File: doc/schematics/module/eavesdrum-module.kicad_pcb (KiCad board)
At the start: 2 copper layers, 100 x 100 mm, 102 parts, among them J1 DC37_Pins_MountingHoles, J2 Conn_02x25_Odd_Even, J3 Conn_01x03, J4 Conn_01x20_Pin, J5 Conn_01x20_Pin, M4_1 MountingHole_4.3mm_M4, M4_2 MountingHole_4.3mm_M4, M4_3 MountingHole_4.3mm_M4, M4_4 MountingHole_4.3mm_M4, SW1 SW_Push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

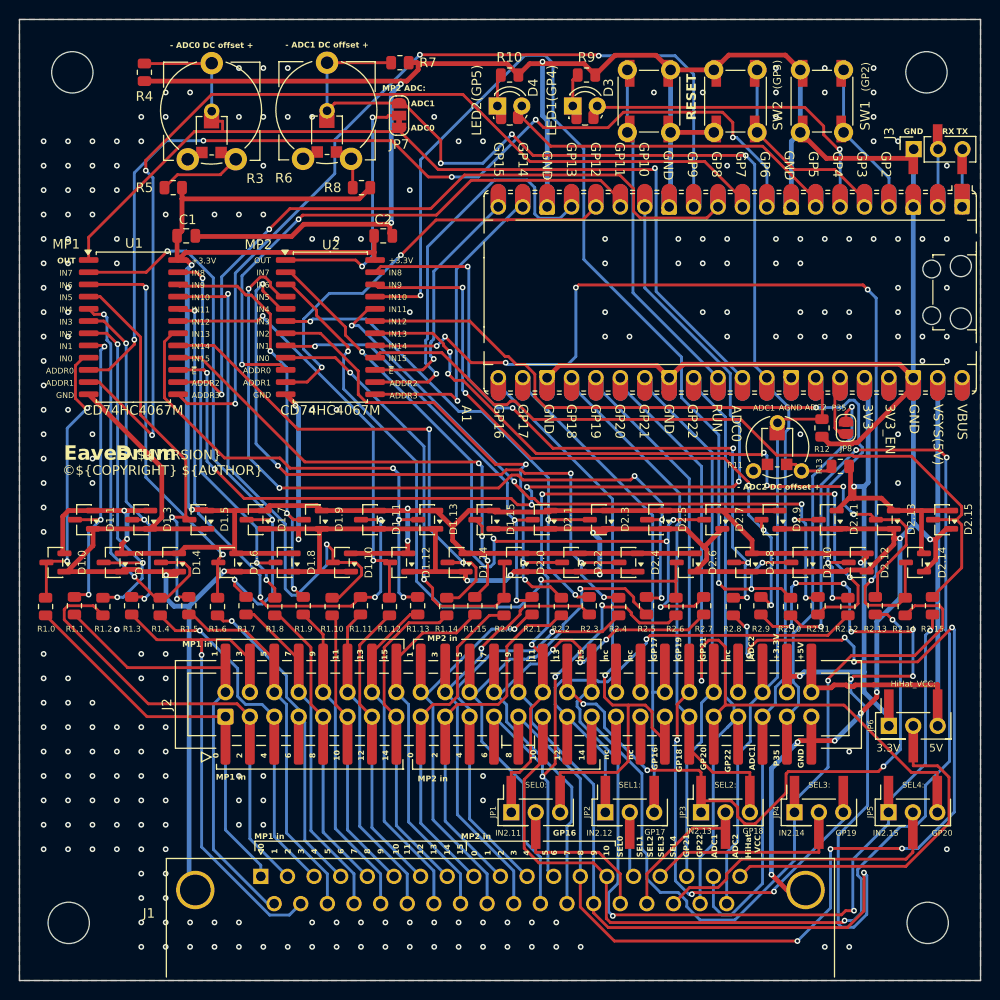
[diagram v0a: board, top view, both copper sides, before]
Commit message: schematics for module 1.2
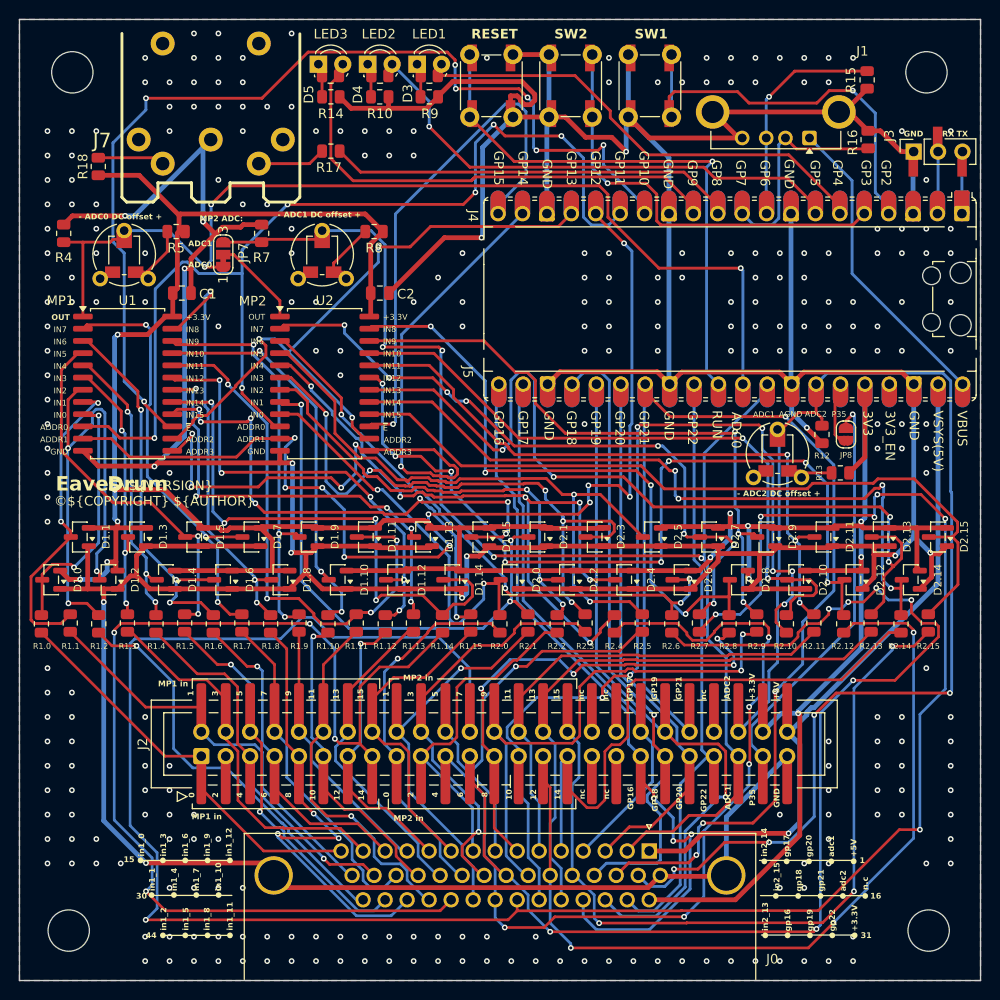
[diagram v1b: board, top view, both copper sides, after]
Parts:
- removed A1: RaspberryPi_Pico, Module:RaspberryPi_Pico_Common_Unspecified
- removed JP1, JP2, JP3, JP4, JP5, JP6: Jumper, Connector_PinHeader_2.54mm:PinHeader_1x03_P2.54mm_Vertical_SMD_Pin1Right
- added D5: LED (yellow), EavesDrum:LED_D3.0mm_SMD_Thru, F.Cu at (97.4, 43.8)
- added J0: SUB-D 44 HD, Connector_Dsub:DSUB-44-HD_Socket_Horizontal_P2.29x2.54mm_EdgePinOffset8.35mm_Housed_MountingHolesOffset10.89mm, F.Cu at (130.5, 124.5)
- added J7: DIN-5_180degree, EavesDrum:MIDI_DIN5, F.Cu at (84.9, 47.5)
- added R14: 4.7k, Resistor_SMD:R_0805_2012Metric, F.Cu at (97.4, 46.1)
- added R15: 15k, Resistor_SMD:R_0805_2012Metric, F.Cu at (153.2, 44.3)
- added R16: 15k, Resistor_SMD:R_0805_2012Metric, F.Cu at (153.3, 50.5)
- added R17: 10, Resistor_SMD:R_0805_2012Metric, F.Cu at (97.4, 51.7)
- added R18: 33, Resistor_SMD:R_0805_2012Metric, F.Cu at (73.2, 53.3)
- D3: footprint LED_THT:LED_D3.0mm -> EavesDrum:LED_D3.0mm_SMD_Thru
- D4: value LED (blue) -> LED (white/blue); footprint LED_THT:LED_D3.0mm -> EavesDrum:LED_D3.0mm_SMD_Thru
- J1: value DC37_Pins_MountingHoles -> USB_A; footprint Connector_Dsub:DSUB-37_Pins_Horizontal_P2.77x2.84mm_EdgePinOffset7.70mm_Housed_MountingHolesOffset9.12mm -> Connector_USB:USB_A_Connfly_DS1095
- J2: footprint Connector_IDC:IDC-Header_2x25_P2.54mm_Vertical -> EavesDrum:IDC-Header_2x25_P2.54mm_Vertical_SMD_Thru
- J3: footprint Connector_PinSocket_2.54mm:PinSocket_1x03_P2.54mm_Vertical_SMD_Pin1Left -> EavesDrum:PinSocket_1x03_P2.54mm_Vertical_SMD_Thru_Pin1Left
- J4: value Conn_01x20_Pin -> Conn_01x20_Socket; footprint Connector_PinSocket_2.54mm:PinSocket_1x20_P2.54mm_Vertical -> EavesDrum:RaspberryPi_Pico_wo_2nd_pin_row
- J5: value Conn_01x20_Pin -> Conn_01x20_Socket; footprint Connector_PinSocket_2.54mm:PinSocket_1x20_P2.54mm_Vertical -> EavesDrum:RaspberryPi_Pico_Common_2nd_pin_row
- R10: value 4.7k -> 10k
- R11, R3, R6: footprint Potentiometer_SMD:Potentiometer_ACP_CA9-VSMD_Vertical -> EavesDrum:Potentiometer_SMD_Thru_Vertical
- SW1, SW2, SW3: footprint Button_Switch_SMD:SW_Push_1P1T_NO_CK_KSC6xxJ -> EavesDrum:SW_Push_SMD_Thru
- moved J1 95.7 mm to (147.2, 50.3), turned to 180 degrees
- moved J5 25.6 mm to (139.0, 67.1), turned to -90 degrees
- moved J4 24.2 mm to (138.9, 58.2)
- moved JP7 23.3 mm to (86.2, 62.5)
- moved R7 22.9 mm to (90.2, 60.3), turned to -90 degrees
- moved R4 18.7 mm to (69.6, 60.3), turned to -90 degrees
- moved SW1 18.0 mm to (130.6, 44.9)
- moved SW2 17.2 mm to (122.3, 44.9)
- moved D3 16.8 mm to (107.6, 43.8)
- moved R9 16.5 mm to (107.6, 46.1)
- moved SW3 16.5 mm to (114.1, 44.9)
- moved D4 14.2 mm to (102.5, 43.8)
- moved R10 13.7 mm to (102.5, 46.1)
- moved R3 13.5 mm to (75.9, 60.0)
- moved R6 10.1 mm to (96.5, 60.0)
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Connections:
- J1 pad 1: /in1_0 -> Vbus
- J1 pad 2: /in1_2 -> gpio7
- J1 pad 3: /in1_4 -> gpio6
- J1 pad 4: /in1_6 -> GND
- J1 pad 5: /in1_8 -> GND
- U1 pad 10: gpio6 -> gpio11
- U1 pad 11: gpio7 -> gpio12
- U1 pad 13: gpio9 -> gpio14
- U1 pad 14: gpio8 -> gpio13
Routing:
- net /in2_7: track 55.9 -> 236.0 mm, vias 3 -> 7
- net GND: track 581.3 -> 666.8 mm, vias 238 -> 284
- net gpio7: track 108.9 -> 23.9 mm, vias 2 -> 0
- net /in1_14: track 36.9 -> 119.8 mm, vias 0 -> 4
- net gpio6: track 104.1 -> 24.4 mm, vias 5 -> 1
- net /in2_9: track 134.5 -> 57.0 mm, vias 8 -> 2
- net adc2: track 66.1 -> 142.3 mm, vias 0 -> 4
- net /in2_8: track 124.7 -> 52.0 mm, vias 8 -> 4
- net /in2_6: track 51.0 -> 123.1 mm, vias 3 -> 7
- net gpio12: track 47.1 -> 113.6 mm, vias 2 -> 10
- net gpio21: track 59.4 -> 123.1 mm, vias 0 -> 4
- net gpio11: track 60.2 -> 112.3 mm, vias 2 -> 6
- net /in2_4: track 45.1 -> 94.1 mm, vias 1 -> 5
- net gpio14: track 33.8 -> 82.0 mm, vias 1 -> 5
- net Net-(D2.10-COM): track 113.1 -> 69.0 mm, vias 4 -> 2
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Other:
- board text added: "16"
- board text added: "30"
- board text added: "31"
- board text added: "44"
- board text added: "LED1"
- board text added: "LED2"
- board text added: "LED3"
- board text added: "SW1"
- board text added: "SW2"
- board text added: "adc1"
- board text added: "adc2"
- board text added: "gp16"
- board text added: "gp17"
- board text added: "gp18"
- board text added: "gp19"
- board text added: "gp20"
- board text added: "gp21"
- board text added: "gp22"
- board text added: "in1_0"
- board text added: "in1_1"
- board text added: "in1_10"
- board text added: "in1_11"
- board text added: "in1_12"
- board text added: "in1_2"
- board text added: "in1_3"
- board text added: "in1_4"
- board text added: "in1_5"
- board text added: "in1_6"
- board text added: "in1_7"
- board text added: "in1_8"
- board text added: "in1_9"
- board text added: "in2_13"
- board text added: "in2_14"
- board text added: "in2_15"
- board text added: "n.c"
- board text removed: "(GP2)"
- board text removed: "(GP3)"
- board text removed: "3.3V"
- board text removed: "5V"
- board text removed: "HiHat _VCC"
- board text removed: "HiHat_VCC:"
- board text removed: "IN2.11"
- board text removed: "IN2.12"
- board text removed: "IN2.13"
- board text removed: "IN2.14"
- board text removed: "IN2.15"
- board text removed: "LED1(GP4)"
- board text removed: "LED2(GP5)"
- board text removed: "SEL0"
- board text removed: "SEL0:"
- board text removed: "SEL1"
- board text removed: "SEL1:"
- board text removed: "SEL2"
- board text removed: "SEL2:"
- board text removed: "SEL3"
- board text removed: "SEL3:"
- board text removed: "SEL4"
- board text removed: "SEL4:"
- board text removed: "in2.11"
- board text removed: "in2.12"
- board text removed: "in2.13"
- board text removed: "in2.14"
- board text removed: "in2.15"
- board text removed: "pin21"
- board text removed: "pin22"
- board text removed: "pin24"
- board text removed: "pin25"
- board text removed: "pin26"
